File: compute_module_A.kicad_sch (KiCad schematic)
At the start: 15 parts, among them J8 MagJack, J9 Micro_SD_Card_Det, U4 RT9742GGJ5

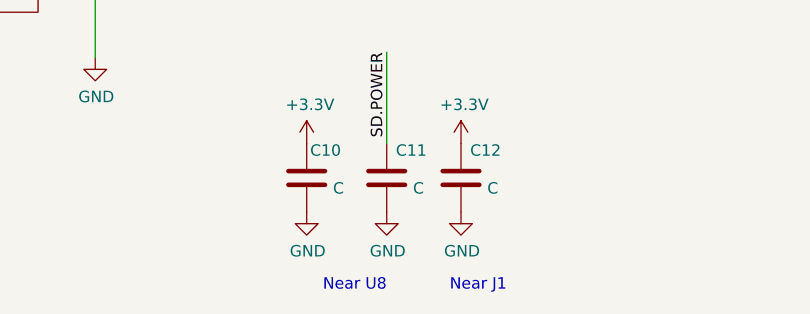
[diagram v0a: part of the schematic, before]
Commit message: Added Daughter Card
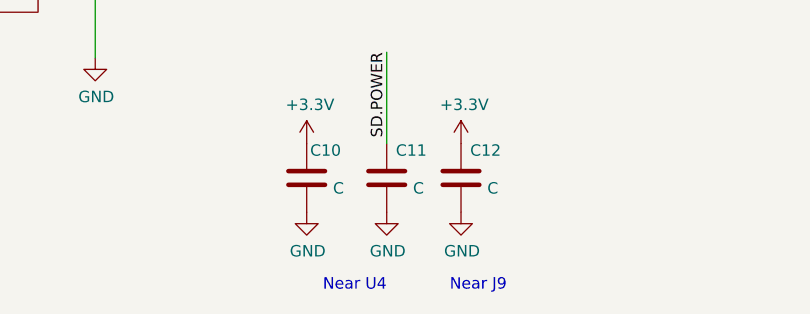
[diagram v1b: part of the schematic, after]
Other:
- note added: "Near J9"
- note added: "Near U4"
- note removed: "Near J1"
- note removed: "Near U8"
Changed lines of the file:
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@@
   (title_block
     (title "Dennis")
-    (date "2020-12-31")
-    (rev "0.1.1")
+    (date "2021-02-26")
+    (rev "0.1.2")
     (company "eCafe Racer")
   )
@@
   (junction (at 184.785 53.975) (diameter 0.9144) (color 0 0 0 0))
   (junction (at 184.785 60.96) (diameter 0.9144) (color 0 0 0 0))
+  (no_connect (at 198.755 66.675))
+  (no_connect (at 33.655 52.07))
+  (no_connect (at 33.655 49.53))
   (no_connect (at 94.615 44.45))
   (no_connect (at 94.615 62.23))
+  (no_connect (at 94.615 41.91))
   (no_connect (at 203.835 66.675))
-  (no_connect (at 94.615 41.91))
-  (no_connect (at 198.755 66.675))
-  (no_connect (at 33.655 52.07))
   (no_connect (at 201.295 66.675))
-  (no_connect (at 33.655 49.53))
   (wire (pts (xy 20.955 133.35) (xy 33.655 133.35))
     (stroke (width 0) (type solid) (color 0 0 0 0))
@@
     (effects (font (size 1.27 1.27)) (justify left bottom))
   )
-  (text "Near U8" (at 130.81 197.485 180)
+  (text "Near U4" (at 130.81 197.485 180)
     (effects (font (size 1.27 1.27)) (justify right bottom))
   )
-  (text "Near J1" (at 144.145 197.485 180)
+  (text "Near J9" (at 144.145 197.485 180)
     (effects (font (size 1.27 1.27)) (justify right bottom))
   )

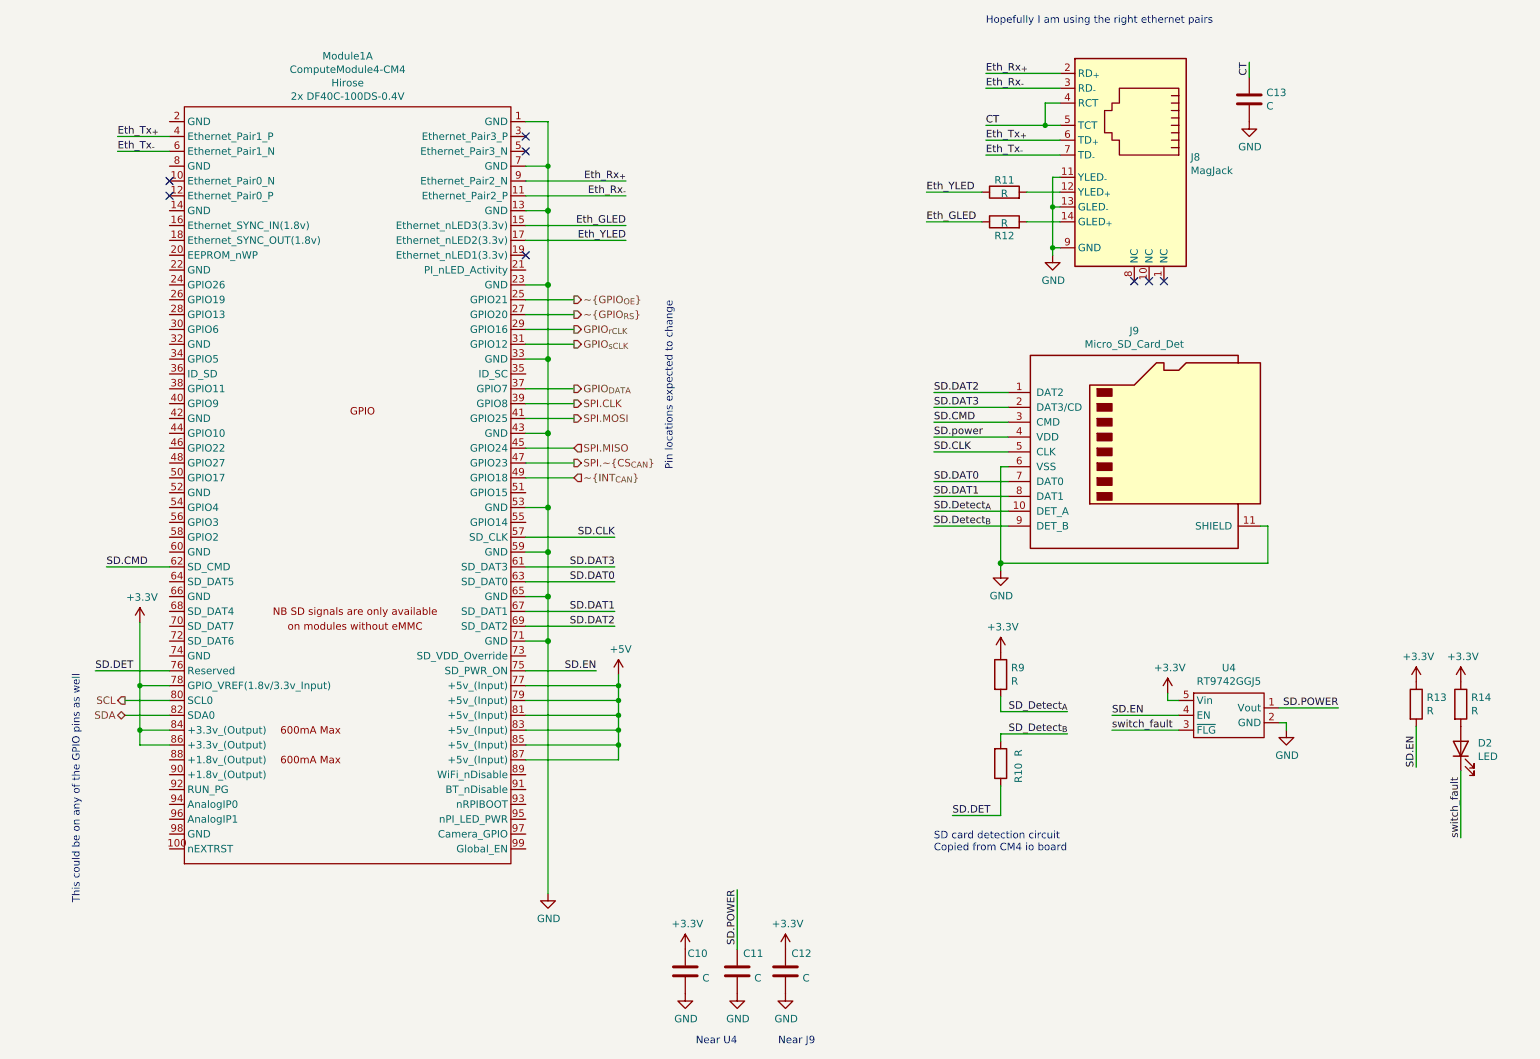
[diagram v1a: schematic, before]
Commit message: more layout: power supply and gpio
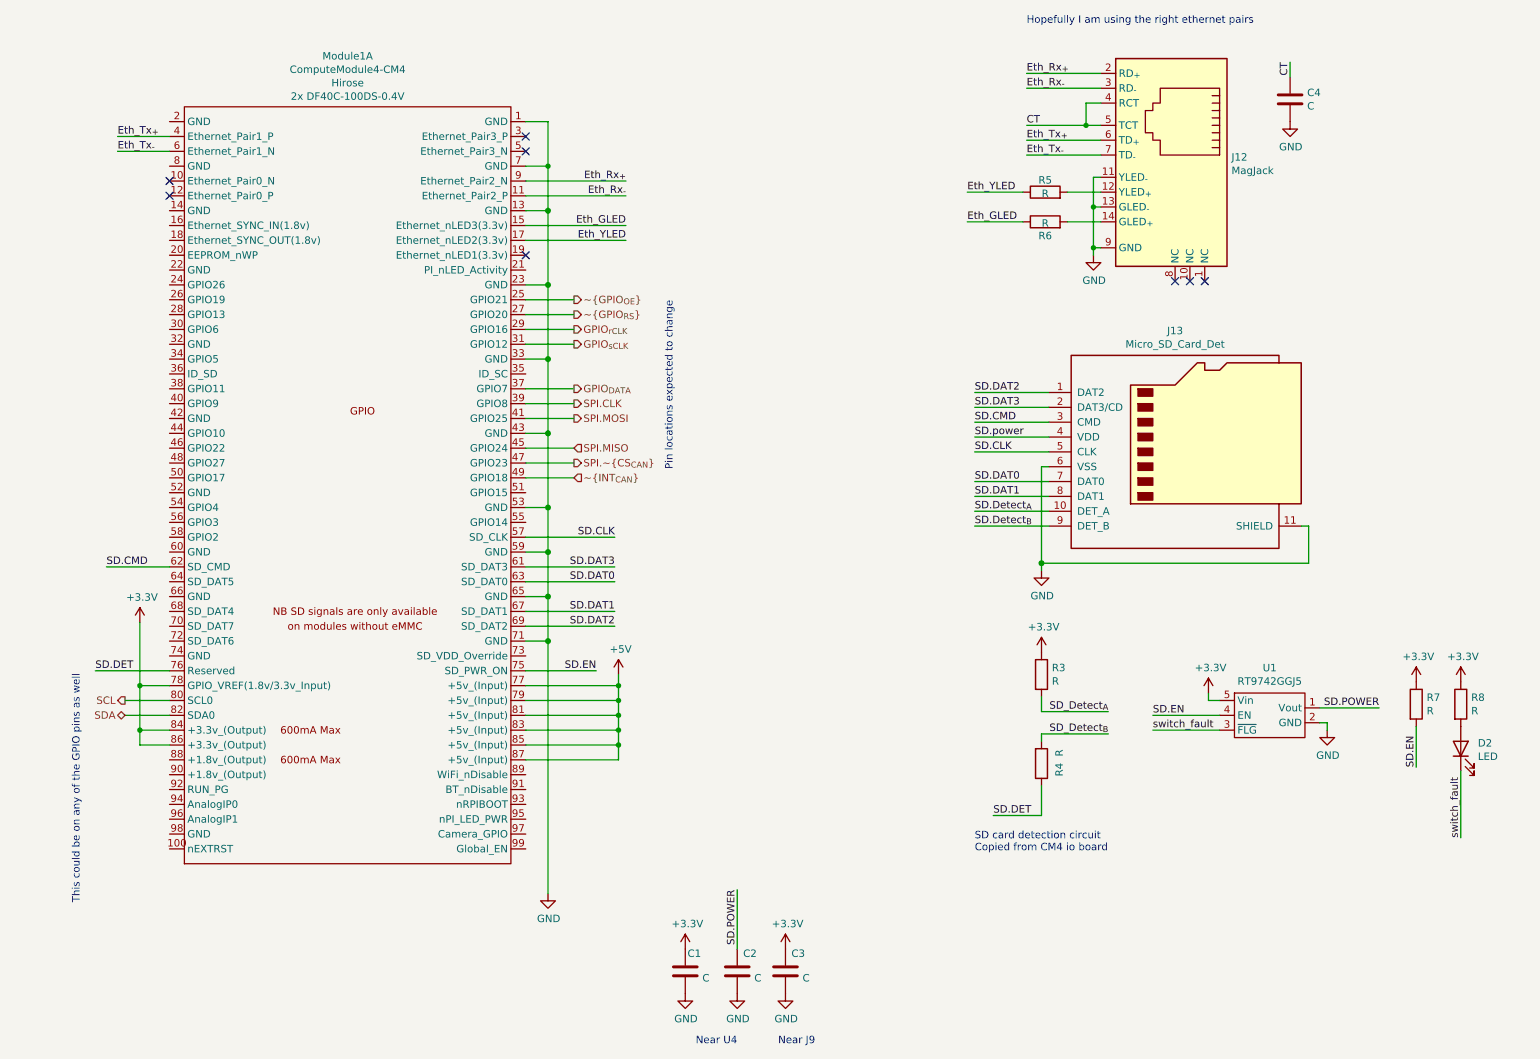
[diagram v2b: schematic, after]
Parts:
- renumbered C10 to C1, C11 to C2, C12 to C3, C13 to C4, J8 to J12, J9 to J13, R9 to R3, R10 to R4, R11 to R5, R12 to R6, R13 to R7, R14 to R8, U4 to U1
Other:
- moved on the sheet: C4, J12, J13, R3, R4, R5, R6, U1

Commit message: Routing for HDMI, Ethernet, SD Card, CAN
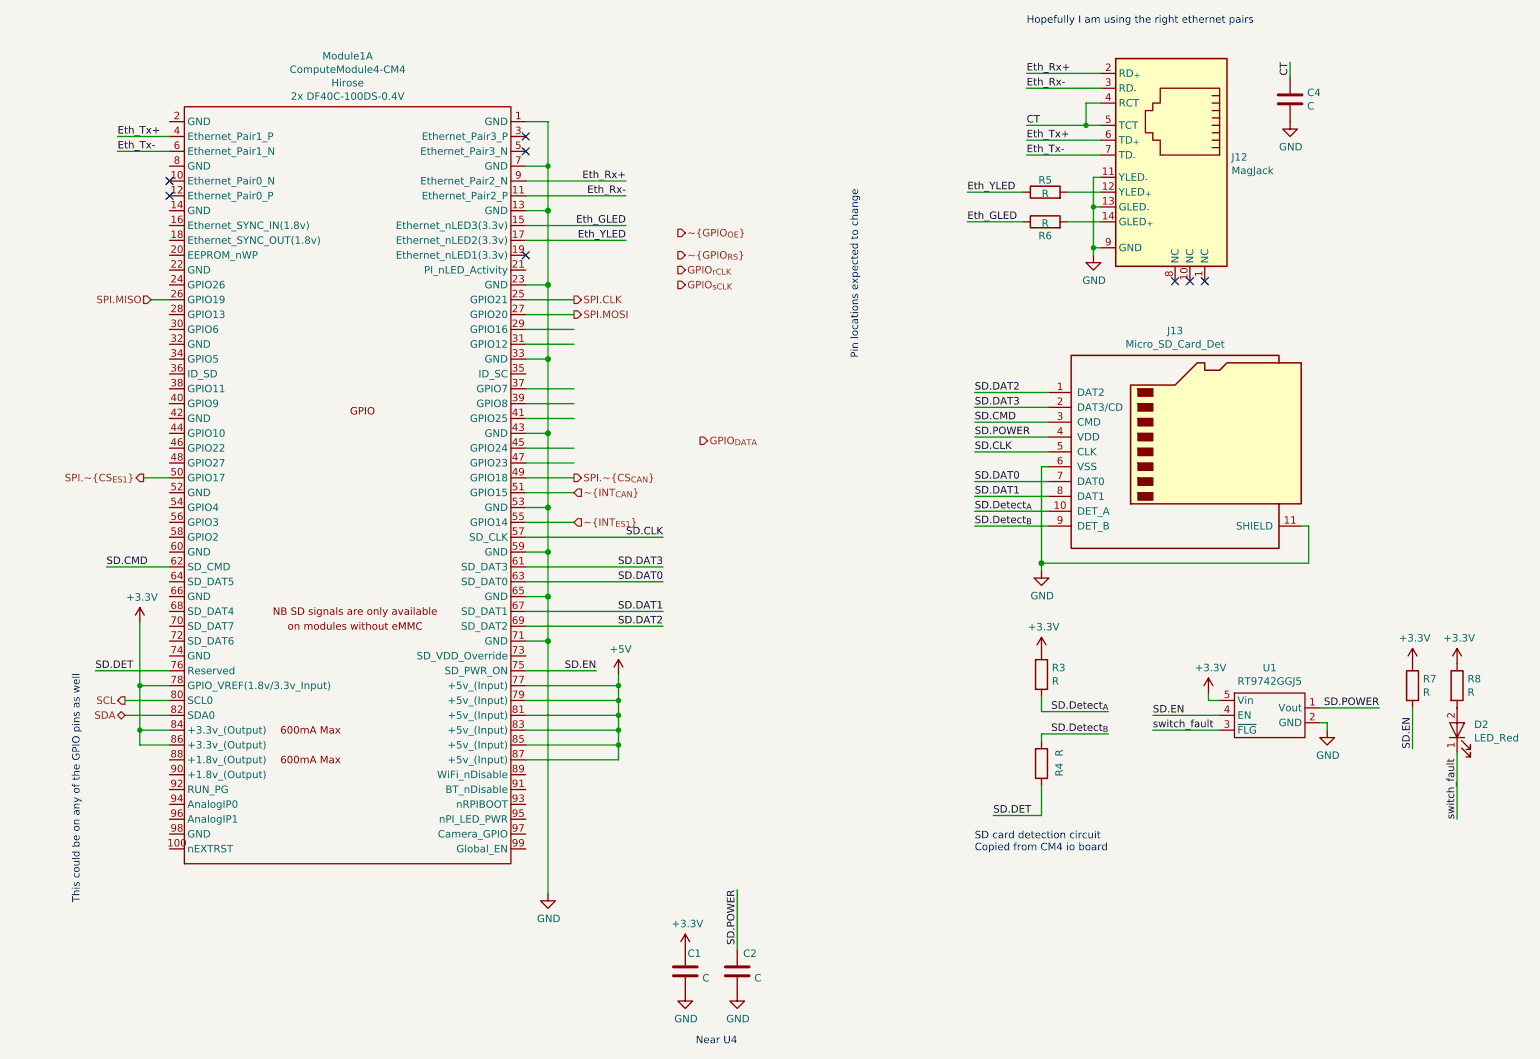
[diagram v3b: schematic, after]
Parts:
- removed C3: C, Capacitor_SMD:C_0805_2012Metric, symbol Device:C
- removed D2: LED, symbol Device:LED
- added D2: LED_Red, LED_SMD:LED_0805_2012Metric_Pad1.15x1.40mm_HandSolder, symbol Custom-Symbols:LED_Red
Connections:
- net SD.power is gone; now on net SD.POWER: J13.4 (VDD)
- net SD_Detect_{A} is gone; now on net SD.Detect_{A}: R3.2
- net SD_Detect_{B} is gone; now on net SD.Detect_{B}: R4.2
- net GPIO_{DATA}: no longer Module1.37 (GPIO7)
- net GPIO_{rCLK}: no longer Module1.29 (GPIO16)
- net GPIO_{sCLK}: no longer Module1.31 (GPIO12)
- net SPI.CLK: now also Module1.25 (GPIO21); no longer Module1.39 (GPIO8)
- net SPI.MISO: now also Module1.26 (GPIO19); no longer Module1.45 (GPIO24)
- net SPI.MOSI: now also Module1.27 (GPIO20); no longer Module1.41 (GPIO25)
- net SPI.~CS_{CAN}: now also Module1.49 (GPIO18); no longer Module1.47 (GPIO23)
- net switch_fault: now also D2.1
- net ~GPIO_{OE}: no longer Module1.25 (GPIO21)
- net ~GPIO_{RS}: no longer Module1.27 (GPIO20)
- net ~INT_{CAN}: now also Module1.51 (GPIO15); no longer Module1.49 (GPIO18)
- net at R8.2: now also D2.2
- net SPI.~CS_{ES1}: now reaches Module1.50 (GPIO17)
- net ~INT_{ES1}: now reaches Module1.55 (GPIO14)
- net Eth_Rx_{+} renamed Eth_Rx+
- net Eth_Rx_{-} renamed Eth_Rx-
- net Eth_Tx_{+} renamed Eth_Tx+
- net Eth_Tx_{-} renamed Eth_Tx-
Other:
- note removed: "Near J9"
- moved on the sheet: R7, R8

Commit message: Finished trace routing
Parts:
- renumbered C4 to C3, D2 to D4, R8 to R10, R3 to R5, R4 to R6, R5 to R7, R6 to R8, R7 to R9
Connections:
- net GND: now also Module1.14 (GND), Module1.2 (GND), Module1.22 (GND), Module1.32 (GND), Module1.42 (GND), Module1.52 (GND), Module1.60 (GND), Module1.66 (GND), Module1.74 (GND), Module1.8 (GND), Module1.98 (GND)
- net GPIO_{DATA}: now also Module1.40 (GPIO9)
- net GPIO_{rCLK}: now also Module1.30 (GPIO6)
- net GPIO_{sCLK}: now also Module1.28 (GPIO13)
- net SCL: now also Module1.56 (GPIO3); no longer Module1.80 (SCL0)
- net SDA: now also Module1.58 (GPIO2); no longer Module1.82 (SDA0)
- net ~GPIO_{OE}: now also Module1.34 (GPIO5)
- net ~GPIO_{RS}: now also Module1.38 (GPIO11)
- net ES.GPIO_{4}: now reaches Module1.29 (GPIO16)
- net ES.GPIO_{5}: now reaches Module1.31 (GPIO12)
- net ES.GPIO_{1}: now reaches Module1.37 (GPIO7)
- net ES.GPIO_{2}: now reaches Module1.39 (GPIO8)
- net ES.GPIO_{3}: now reaches Module1.41 (GPIO25)
- no-connect marks 8 -> 10
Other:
- note removed: "This could be on any of the GPIO pins as well"
- moved on the sheet: Module1A
